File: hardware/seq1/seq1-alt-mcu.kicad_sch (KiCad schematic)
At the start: 1 part

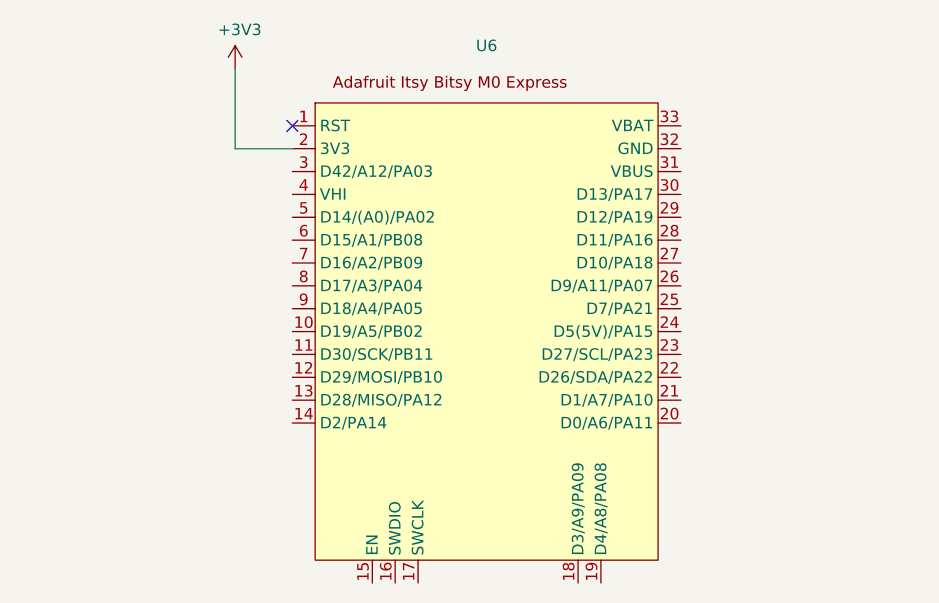
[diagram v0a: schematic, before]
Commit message: updates to schematic/layout (started layout). Added glyph and display class to manage and show status (PoC)
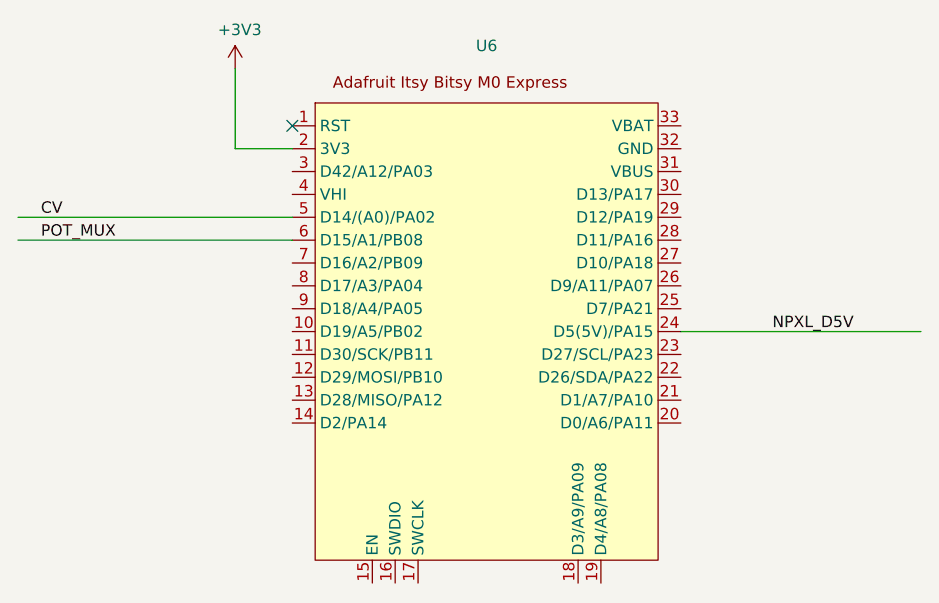
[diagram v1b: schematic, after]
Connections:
- net NPXL_D5V: now reaches U6.24 (D5(5V)/PA15)
- net CV: now reaches U6.5 (D14/(A0)/PA02)
- net POT_MUX: now reaches U6.6 (D15/A1/PB08)
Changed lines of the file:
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@@
+	(wire
+		(pts
+			(xy 49.53 67.31) (xy 80.01 67.31)
+		)
+		(stroke
+			(width 0)
+			(type default)
+		)
+	)
+	(wire
+		(pts
+			(xy 49.53 64.77) (xy 80.01 64.77)
+		)
+		(stroke
+			(width 0)
+			(type default)
+		)
+	)
+	(wire
+		(pts
+			(xy 123.19 77.47) (xy 149.86 77.47)
+		)
+		(stroke
+			(width 0)
+			(type default)
+		)
+	)
 	(wire
 		(pts
@@
 		)
 	)
+	(label "POT_MUX"
+		(at 52.07 67.31 0)
+		(fields_autoplaced yes)
+		(effects
+			(font
+				(size 1.27 1.27)
+			)
+			(justify left bottom)
+		)
+	)
+	(label "NPXL_D5V"
+		(at 133.35 77.47 0)
+		(fields_autoplaced yes)
+		(effects
+			(font
+				(size 1.27 1.27)
+			)
+			(justify left bottom)
+		)
+	)
+	(label "CV"
+		(at 52.07 64.77 0)
+		(fields_autoplaced yes)
+		(effects
+			(font
+				(size 1.27 1.27)
+			)
+			(justify left bottom)
+		)
+	)
